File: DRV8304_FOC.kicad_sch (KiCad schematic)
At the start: 64 parts, among them J1 Conn_01x02, J2 Conn_01x03, J3 Conn_01x03, Q1 SIRA18ADP, Q2 SIRA18ADP, Q3 SIRA18ADP, Q4 SIRA18ADP, Q5 SIRA18ADP, Q6 SIRA18ADP, SW2 SW_Push, U1 TPS565208, U2 TPS259850RQPR, U3 DRV8304HRHAR, U4 STM32F412CEUx, U5 AS5055A, Y1 Crystal_GND23

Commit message: hall sensor
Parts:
- added C29: 4.7uF, Capacitor_SMD:C_0603_1608Metric, symbol Device:C
- added C30: 100nF, Capacitor_SMD:C_0402_1005Metric, symbol Device:C
- added R10, R22, R9: 22R, Resistor_SMD:R_0402_1005Metric, symbol Device:R
- added R21, R7: 10k, Resistor_SMD:R_0402_1005Metric, symbol Device:R
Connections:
- net 3V3: now also U5.14 (WM), R21.1, R7.1
- net GND: now also U5.10 (~{EN_INT}), U5.13 (VSS), U5.9 (TEST), C29.2, C30.2
- net at U5.1 (MOSI): now also R9.2
- net at U5.11 (VDDp): now also C30.1
- net at U5.12 (VDD): now also C29.1, R7.2
- net ~{INT}: now reaches U5.15 (~{INT})
- net ~{INT}: now also R21.2
- net at U5.2 (MISO): now also R22.1
- net at U5.3 (SCK): now also R10.2
- net ~{SS}: now reaches U5.4 (~{SS})
- new net MISO: R22.2
- new net MOSI: R9.1
- new net SCk: R10.1
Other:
- moved on the sheet: H1, H2, H3

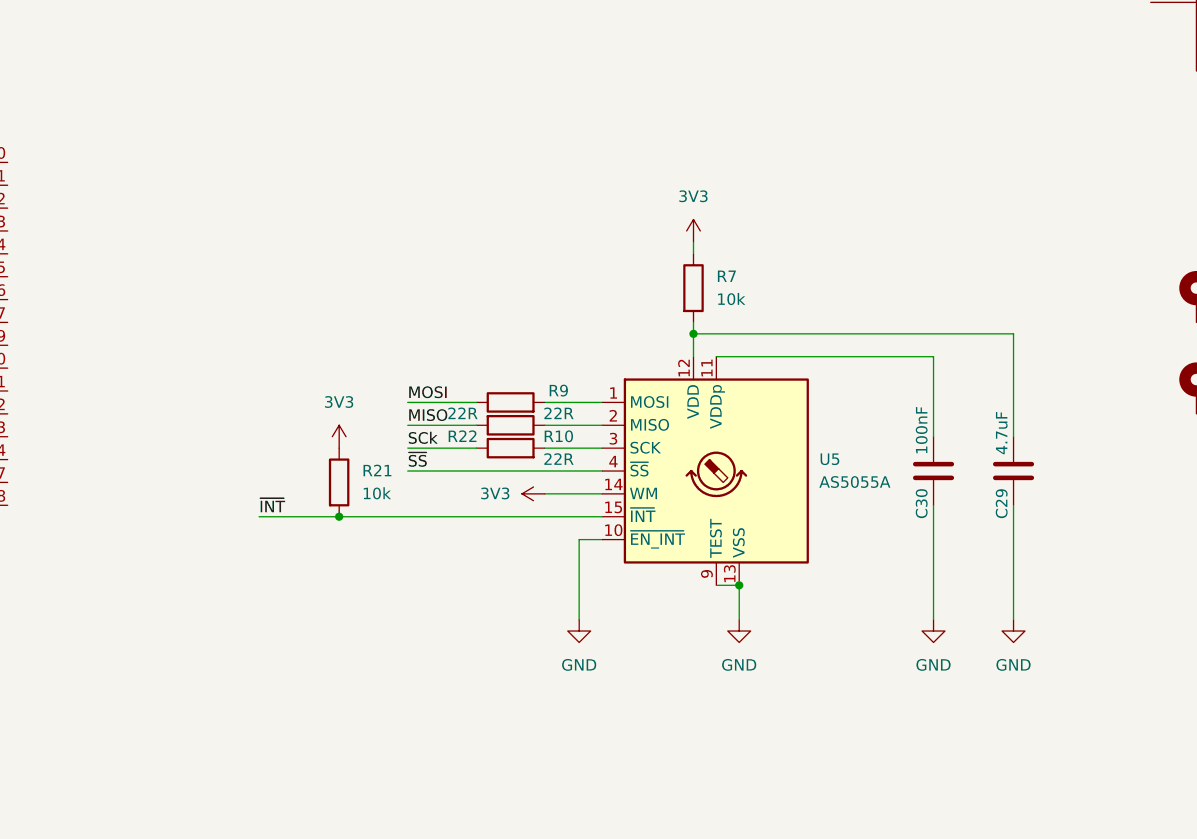
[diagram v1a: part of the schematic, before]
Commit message: Modified encoder sch, modified layout
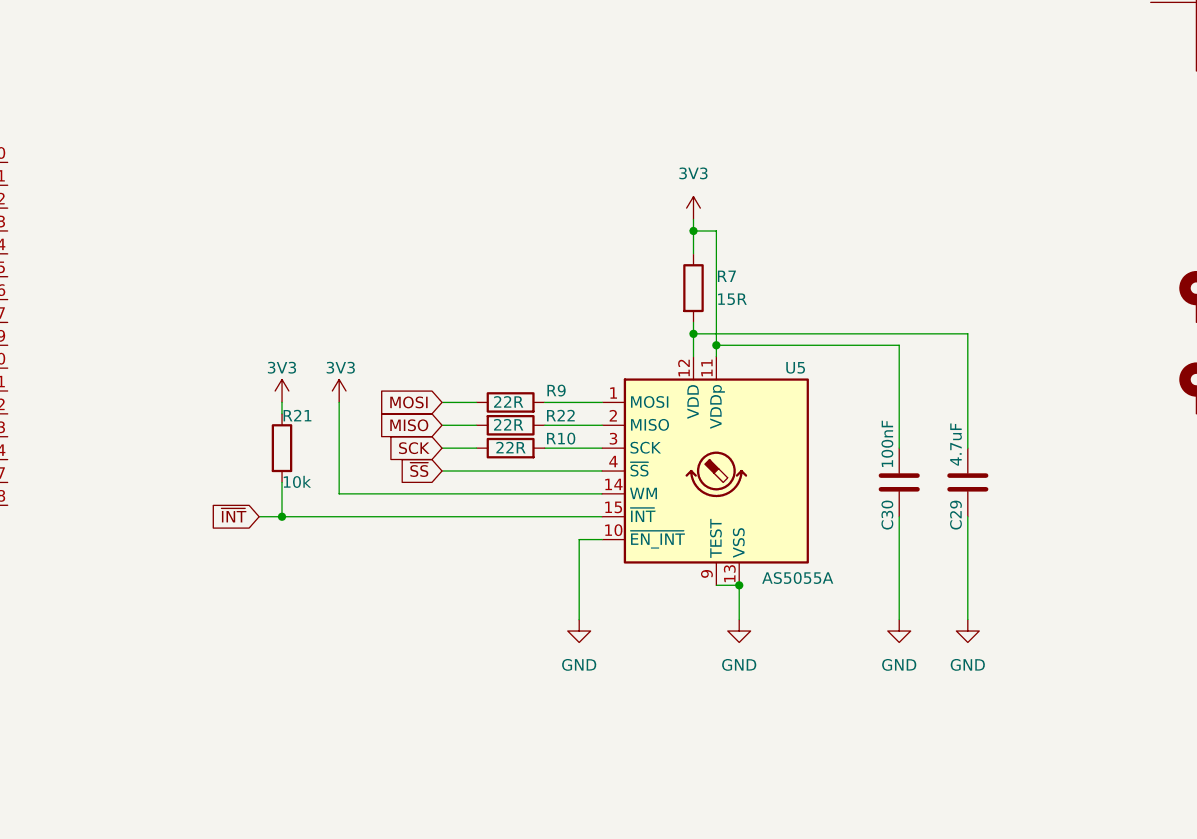
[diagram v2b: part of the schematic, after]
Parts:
- R7: value 10k -> 15R
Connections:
- net 3V3: now also C30.1, U5.11 (VDDp)
- net SCk renamed SCK
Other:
- moved on the sheet: C29, C30, R21

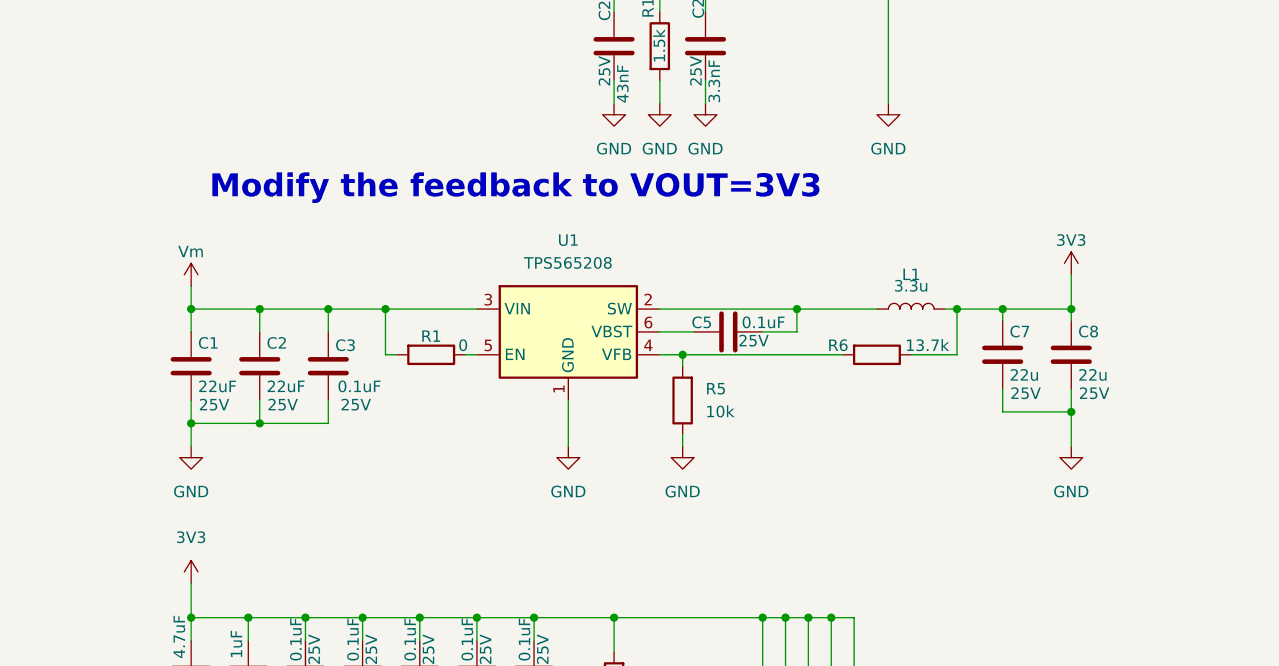
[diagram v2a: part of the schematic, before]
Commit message: Replace buck converter with LDO
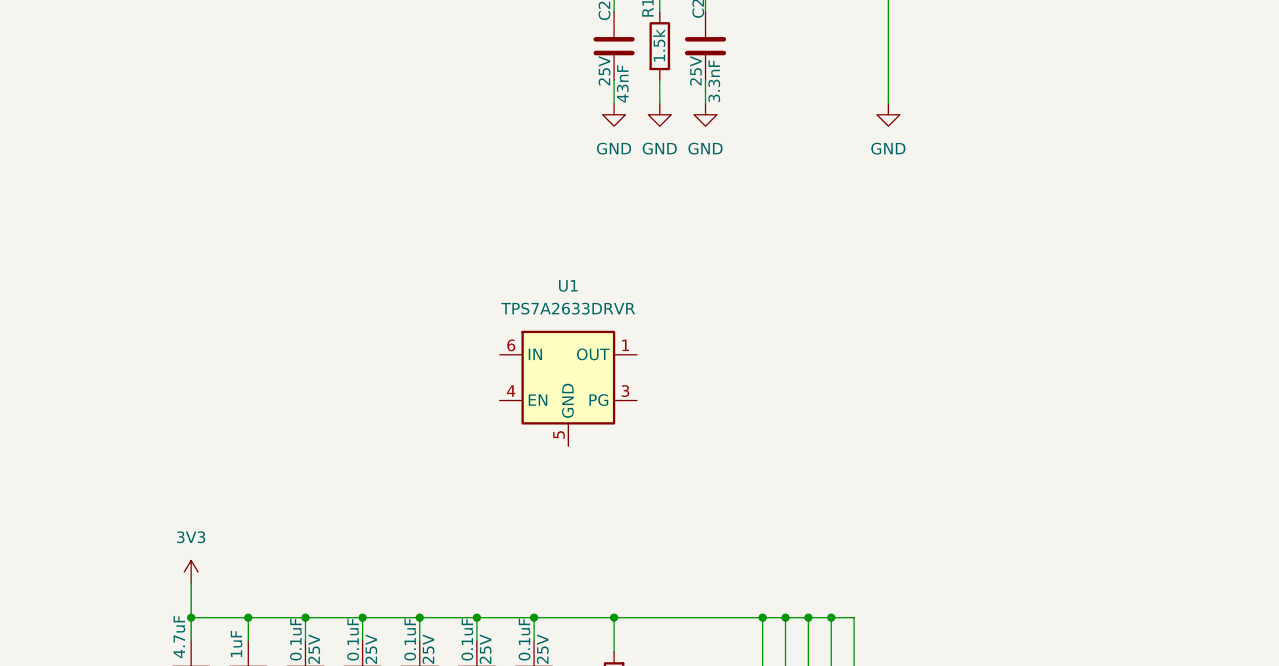
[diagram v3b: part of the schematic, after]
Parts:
- removed C1, C2: 22uF, Capacitor_SMD:C_0805_2012Metric, symbol Device:C
- removed C3, C5: 0.1uF, Capacitor_SMD:C_0402_1005Metric, symbol Device:C
- removed C7, C8: 22u, Capacitor_SMD:C_0805_2012Metric, symbol Device:C
- removed L1: 3.3u, Inductor_SMD:L_APV_APH0420, symbol Device:L
- removed R1: 0, Resistor_SMD:R_0402_1005Metric, symbol Device:R
- removed R5: 10k, Resistor_SMD:R_0402_1005Metric, symbol Device:R
- removed R6: 13.7k, Resistor_SMD:R_0402_1005Metric, symbol Device:R
- removed U1: TPS565208, Package_TO_SOT_SMD:SOT-23-6, symbol Regulator_Switching:TPS565208
- added U1: TPS7A2633DRVR, Package_SON:WSON-6-1EP_2x2mm_P0.65mm_EP1x1.6mm, symbol 1_MyLib:TPS7A26
- H1, H2, H3, H4: footprint MountingHole:MountingHole_2.2mm_M2_Pad -> MountingHole:MountingHole_3.2mm_M3_DIN965_Pad
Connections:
- new net EPAD: U1.5 (GND), U1.7 (EPAD)
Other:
- note removed: "Modify the feedback to VOUT=3V3"

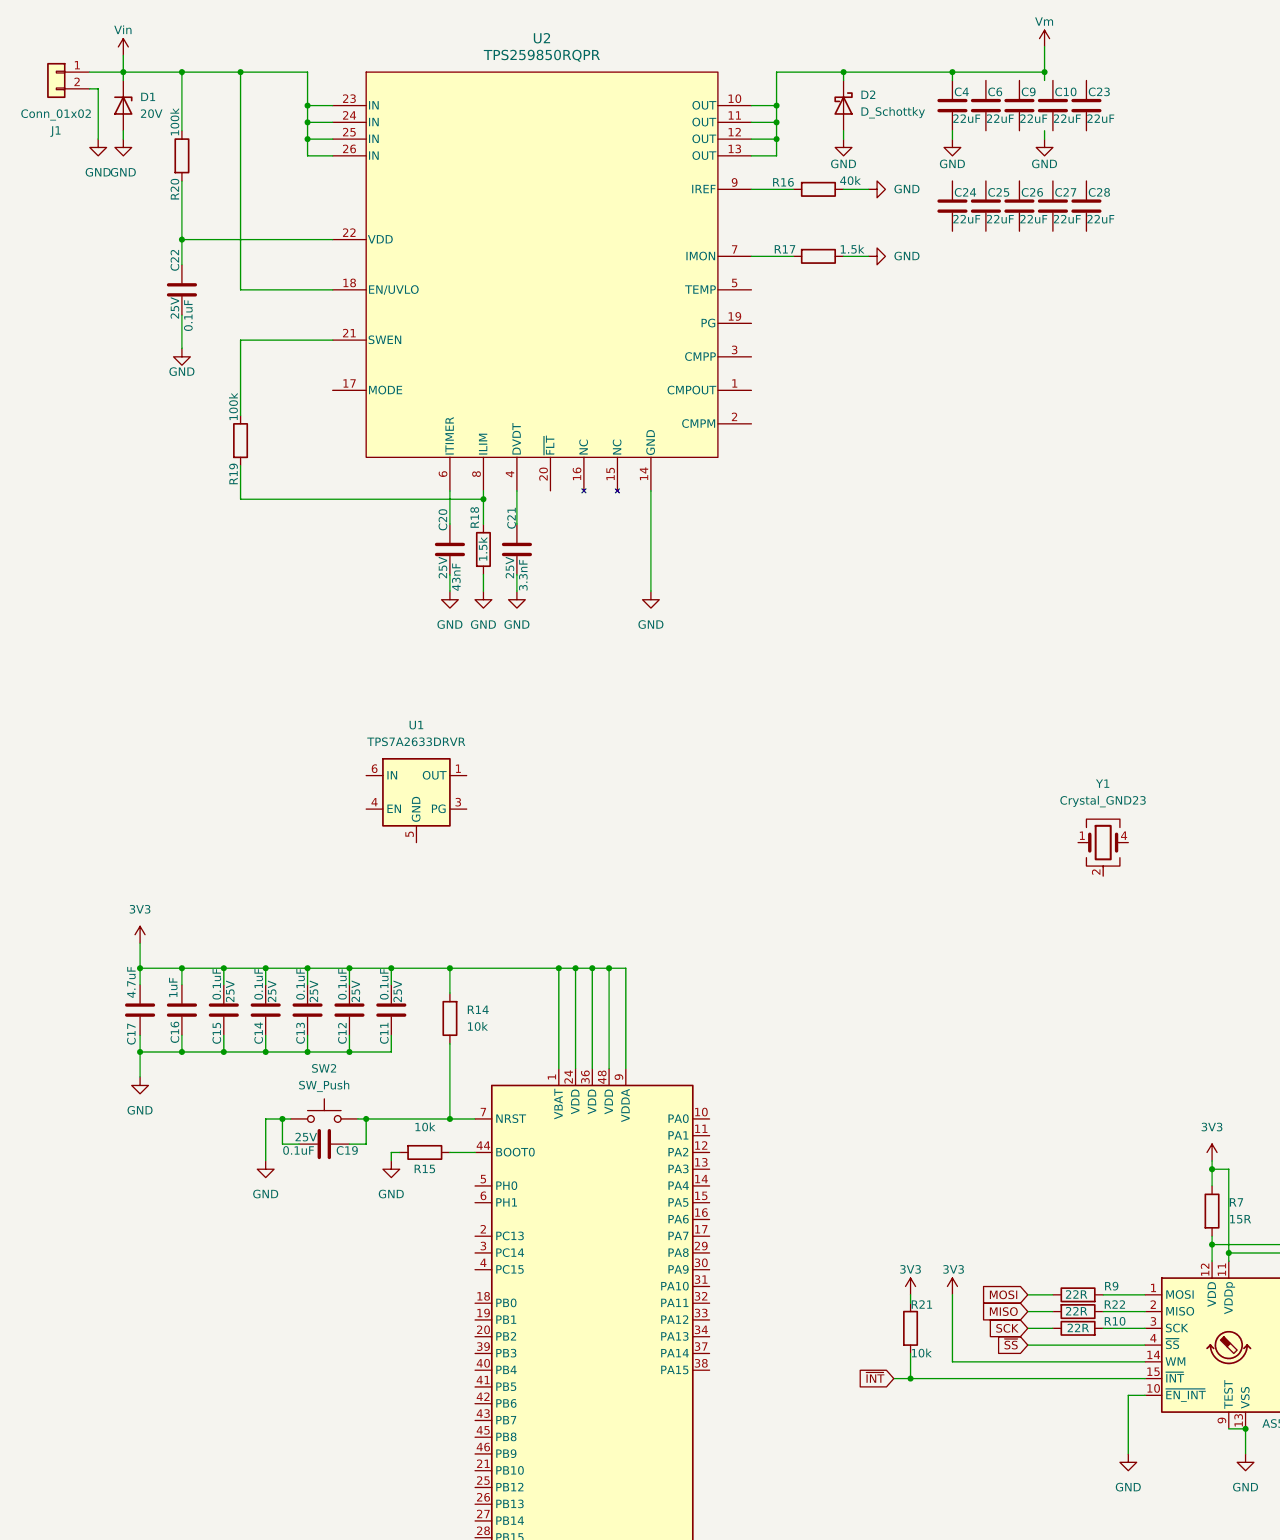
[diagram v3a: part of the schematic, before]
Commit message: Add buck back, changed board shape, replace cer cap with alu cap
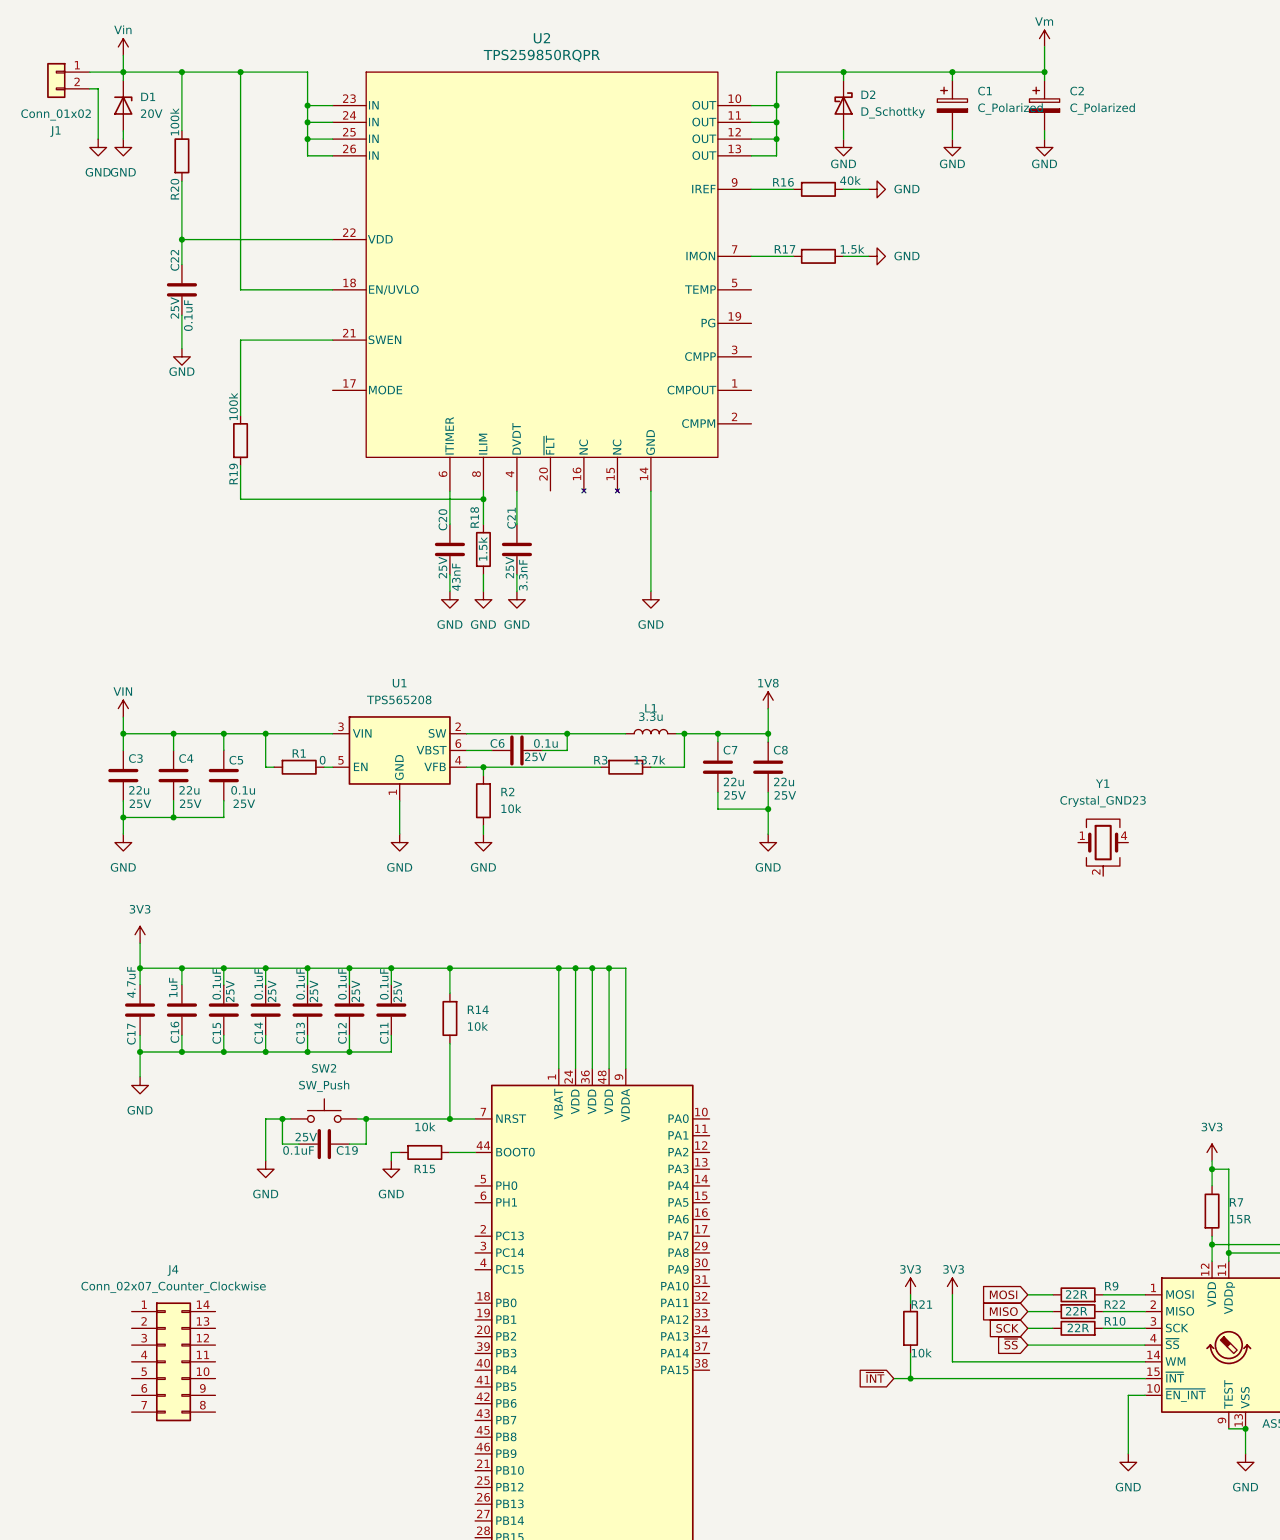
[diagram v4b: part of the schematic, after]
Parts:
- removed C10, C23, C24, C25, C26, C27, C28, C9: 22uF, Capacitor_SMD:C_1206_3216Metric, symbol Device:C
- removed U1: TPS7A2633DRVR, Package_SON:WSON-6-1EP_2x2mm_P0.65mm_EP1x1.6mm, symbol 1_MyLib:TPS7A26
- added C1, C2: C_Polarized, Capacitor_SMD:CP_Elec_6.3x7.7, symbol Device:C_Polarized
- added C3, C7, C8: 22u, Capacitor_SMD:C_0805_2012Metric, symbol Device:C
- added C5: 0.1u, Capacitor_SMD:C_0402_1005Metric, symbol Device:C
- added J4: Conn_02x07_Counter_Clockwise, Connector_PinHeader_1.27mm:PinHeader_2x07_P1.27mm_Vertical_SMD, symbol Connector_Generic:Conn_02x07_Counter_Clockwise
- added L1: 3.3u, Inductor_SMD:L_1008_2520Metric, symbol Device:L
- added R1: 0, Resistor_SMD:R_0402_1005Metric, symbol Device:R
- added R2: 10k, Resistor_SMD:R_0402_1005Metric, symbol Device:R
- added R3: 13.7k, Resistor_SMD:R_0402_1005Metric, symbol Device:R
- added U1: TPS565208, Package_TO_SOT_SMD:SOT-23-6, symbol Regulator_Switching:TPS565208
- C4: value 22uF -> 22u; footprint Capacitor_SMD:C_1206_3216Metric -> Capacitor_SMD:C_0805_2012Metric; Voltage Rating (none) -> 25V
- C6: value 22uF -> 0.1u; footprint Capacitor_SMD:C_1206_3216Metric -> Capacitor_SMD:C_0402_1005Metric; Voltage Rating (none) -> 25V
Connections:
- net GND: now also C1.2, C2.2, C3.2, C5.2, C7.2, C8.2, R2.1, U1.1 (GND)
- net Vm: now also C1.1, C2.1; no longer C4.1
- net at C6.1: now also U1.6 (VBST)
- net at C6.2: now also L1.1, U1.2 (SW)
- new net: R2.2, R3.2, U1.4 (VFB)
- new net: R1.1, U1.5 (EN)
- new net 1V8: C7.1, C8.1, L1.2, R3.1
- new net VIN: C3.1, C4.1, C5.1, R1.2, U1.3 (VIN)
